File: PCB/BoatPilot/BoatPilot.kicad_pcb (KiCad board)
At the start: 4 copper layers, 65 x 35.5 mm, 125 parts, among them J101 battery, J102 Raspberry_Pi_2_3, J103 FlexInput, J104 out 1, J105 SWD, J106 out 2, J107 out 3, J108 UART, J109 out 4, J110 out 5, J111 out 6, J112 GPS, J113 I2C Flex, J114 wind, J115 ANT, J116 USB_OTG, J117 Micro_SD_Card, P101 ICT-Point, P102 ICT-Point, P104 ICT-Point, P105 ICT-Point, P106 ICT-Point, P107 ICT-Point, P108 ICT-Point, P109 ICT-Point, P110 ICT-Point, P111 ICT-Point, P112 ICT-Point, Q101 TSM3457, U101 TPS565208, U102 TLV75733PDBV, U103 TLV75733PDBV, U104 BMX160, U105 STM32F405RGTx, U106 74LVC1G86, U107 P-SENSE, U108 W25Q128JVS, U109 TLV75733PDBV, U111 RFM69HW, Y101 8MHz

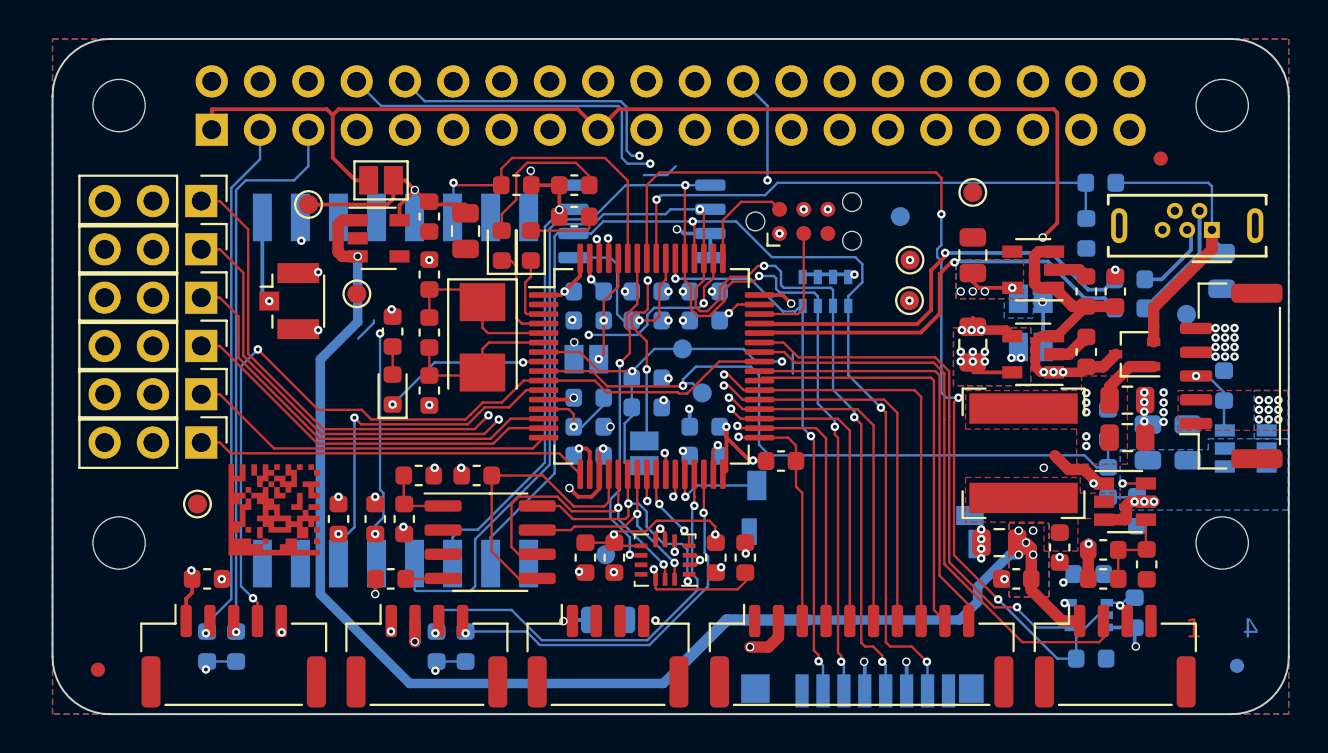
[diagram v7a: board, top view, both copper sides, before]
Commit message: Fix blunder in layout
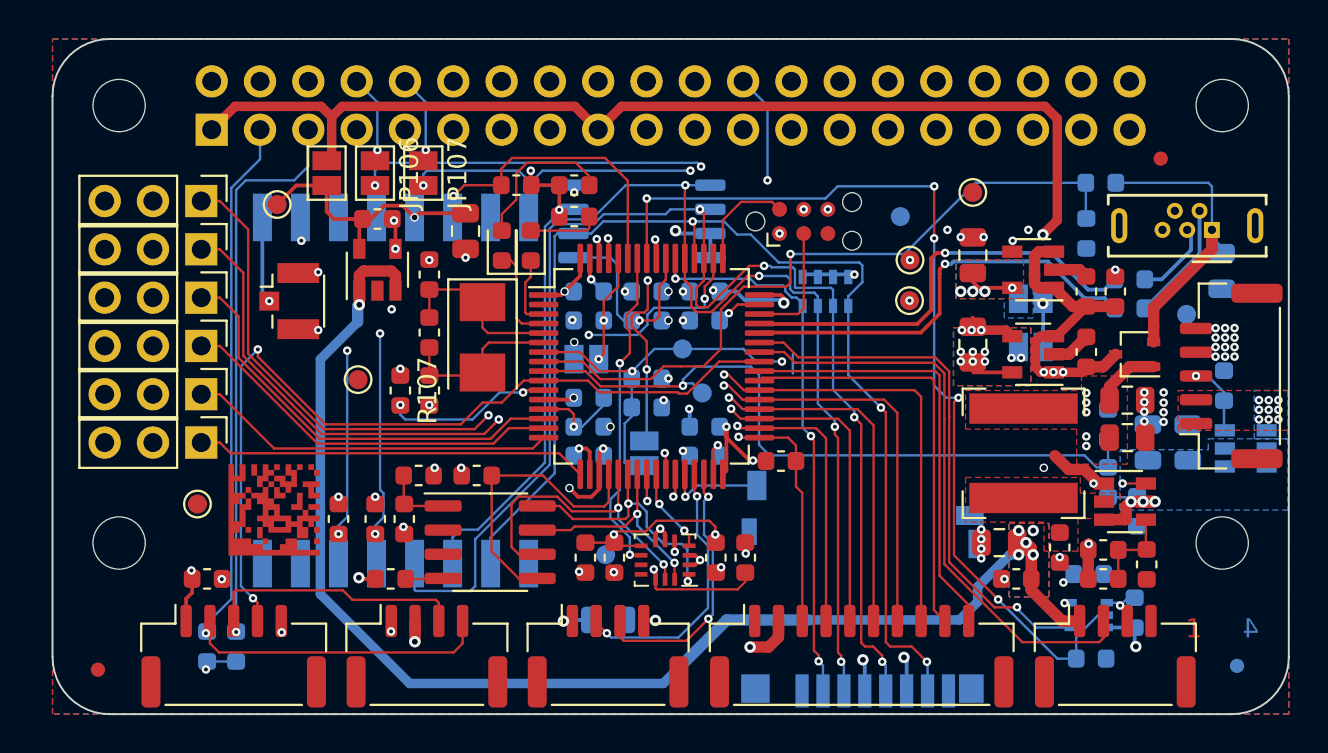
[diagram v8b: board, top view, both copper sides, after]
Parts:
- removed D104: LED, LED_SMD:LED_0603_1608Metric
- removed R125, R126: 2.2k, Resistor_SMD:R_0603_1608Metric
- added JP106: UART_TX, Jumper:SolderJumper-2_P1.3mm_Open_Pad1.0x1.5mm, F.Cu at (29.5, 31.6)
- added JP107: UART_RX, Jumper:SolderJumper-2_P1.3mm_Open_Pad1.0x1.5mm, F.Cu at (32.0, 31.6)
- R107: value 2.2k -> 10k
- moved P105 4.51 mm to (28.6, 42.4)
- moved R107 3.13 mm to (30.8, 43.0), turned to 270 degrees
- moved JP102 2.88 mm to (26.9, 31.6), turned to 270 degrees
- moved C131 2.73 mm to (29.6, 34.0), turned to 180 degrees
- moved U109 1.65 mm to (29.6, 36.6), turned to 90 degrees
- moved P112 1.65 mm to (24.3, 33.2)
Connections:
- J102 pad 10: /UART6_TX -> Net-(J102-Pad10)
- J102 pad 11: Net-(J102-Pad11) -> (no net)
- J102 pad 12: Net-(J102-Pad12) -> (no net)
- J102 pad 13: Net-(J102-Pad13) -> (no net)
- J102 pad 16: Net-(J102-Pad16) -> (no net)
- J102 pad 18: Net-(J102-Pad18) -> (no net)
- J102 pad 22: Net-(J102-Pad22) -> (no net)
- J102 pad 26: Net-(J102-Pad26) -> (no net)
- J102 pad 27: Net-(J102-Pad27) -> (no net)
- J102 pad 28: Net-(J102-Pad28) -> (no net)
- J102 pad 29: Net-(J102-Pad29) -> (no net)
- J102 pad 31: Net-(J102-Pad31) -> (no net)
- J102 pad 32: Net-(J102-Pad32) -> (no net)
- J102 pad 33: Net-(J102-Pad33) -> (no net)
- J102 pad 35: Net-(J102-Pad35) -> (no net)
- J102 pad 36: Net-(J102-Pad36) -> (no net)
- J102 pad 37: Net-(J102-Pad37) -> (no net)
- J102 pad 38: Net-(J102-Pad38) -> (no net)
- J102 pad 40: Net-(J102-Pad40) -> (no net)
- J102 pad 7: Net-(J102-Pad7) -> (no net)
- J102 pad 8: /UART6_RX -> Net-(J102-Pad8)
- J105 pad 5: Net-(J105-Pad5) -> (no net)
- J112 pad 2: /UART2_TX -> /UART3_TX
- J112 pad 3: /UART2_RX -> /UART3_RX
- J113 pad 3: /I2C2_SCL -> /I2C1_SCL
- J113 pad 4: /I2C2_SDA -> /I2C1_SDA
- J116 pad 4: Net-(J116-Pad4) -> (no net)
- J117 pad 1: Net-(J117-Pad1) -> (no net)
- J117 pad 8: Net-(J117-Pad8) -> (no net)
- R107 pad 1: Net-(D104-Pad2) -> +3V3
- R107 pad 2: +3V3 -> /5V_SENSE
- U105 pad 11: /RFM_RST -> /5V_SENSE
- U105 pad 2: Net-(U105-Pad2) -> (no net)
- U105 pad 29: /I2C2_SCL -> /UART3_TX
- U105 pad 30: /I2C2_SDA -> /UART3_RX
- U105 pad 56: /VBUS_SENSE -> /RFM_RST
- U105 pad 8: Net-(D104-Pad1) -> /VBUS_SENSE
- U111 pad 11: Net-(U111-Pad11) -> (no net)
- U111 pad 12: Net-(U111-Pad12) -> (no net)
- U111 pad 15: Net-(U111-Pad15) -> (no net)
- U111 pad 16: Net-(U111-Pad16) -> (no net)
- U111 pad 7: Net-(U111-Pad7) -> (no net)
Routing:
- net /I2C2_SCL: track 22.8 -> 0.00 mm, vias 2 -> 0
- net /I2C2_SDA: track 20.8 -> 0.00 mm, vias 2 -> 0
- net /I2C1_SDA: track 51.7 -> 67.7 mm
- net /RFM_RST: track 19.1 -> 33.7 mm, vias 2 -> 3
- net /UART3_TX: track 0.00 -> 14.3 mm, vias 0 -> 2
- net /UART3_RX: track 0.00 -> 14.1 mm, vias 0 -> 2
- net /I2C1_SCL: track 51.3 -> 64.9 mm
- net /VBUS_SENSE: track 27.9 -> 37.1 mm
- net Net-(D104-Pad1): track 8.87 -> 0.00 mm, vias 2 -> 0
- net /5V_SENSE: track 0.00 -> 8.81 mm, vias 0 -> 2
- net Net-(J102-Pad8): track 0.00 -> 4.68 mm, vias 0 -> 1
- net Net-(J102-Pad10): track 0.00 -> 4.68 mm, vias 0 -> 1
- net /UART6_TX: track 52.2 -> 48.3 mm, vias 2 -> 3
- net /UART6_RX: track 56.4 -> 52.7 mm, vias 2 -> 3
- net +3.3VP: track 64.2 -> 61.8 mm
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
